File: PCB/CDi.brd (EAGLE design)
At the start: 58.5 x 61 mm, 9 parts, among them U1 SN74AHCT125N, U2 SN74AHCT125N

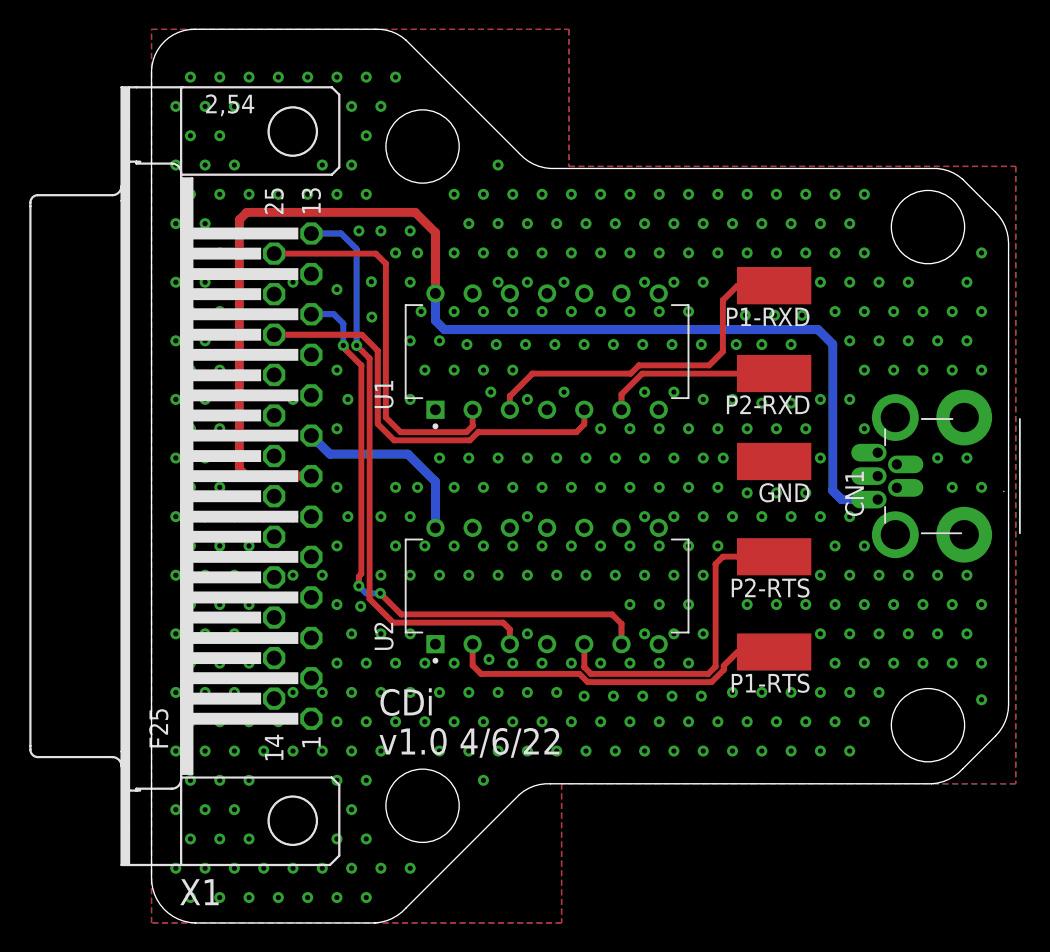
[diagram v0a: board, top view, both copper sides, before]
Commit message: CD-i PCB/BOM Update
Identified USB Mini from Digikey and add it to the BOM.

Updated the PCB to match the layout for the USB Mini Connector and added a callout on the PCB that the connector is required for 5V Power.

Updated project status to include the complete PC-FX Status.
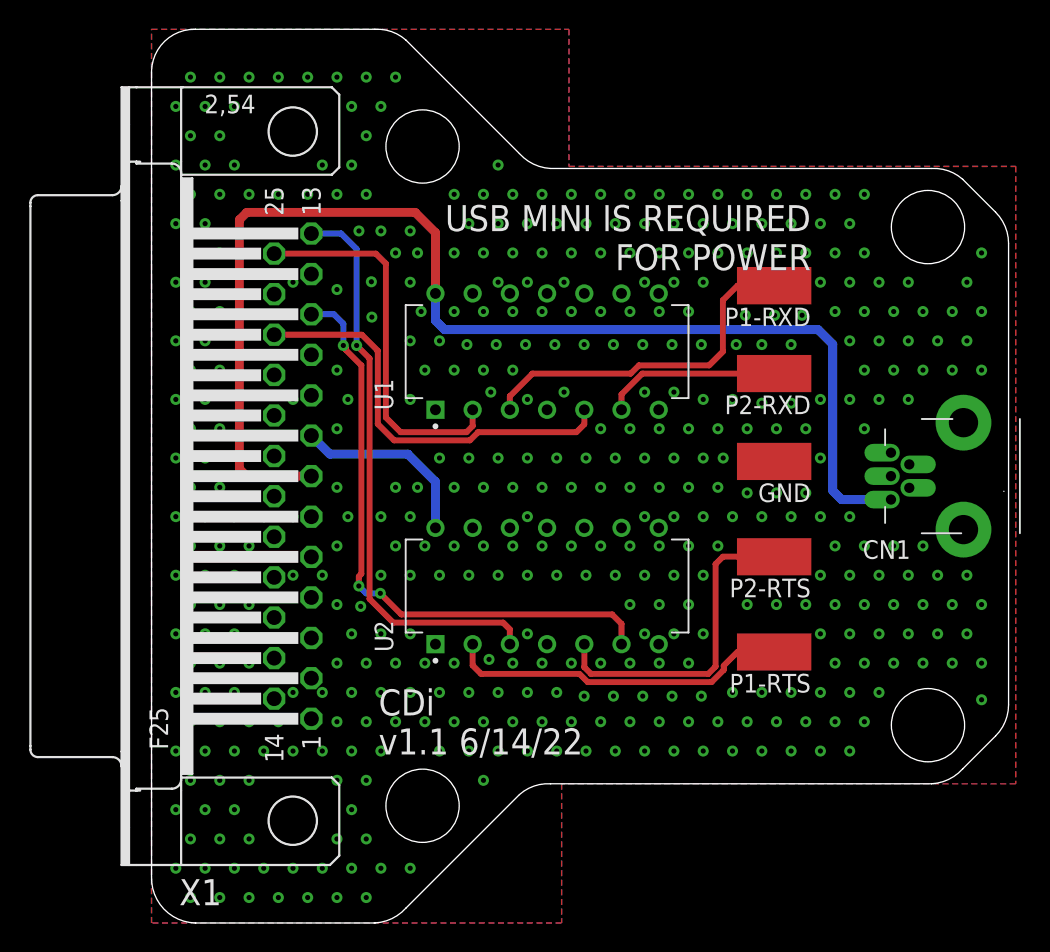
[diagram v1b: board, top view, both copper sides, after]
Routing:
- net 5VIN: track 83.4 -> 84.3 mm
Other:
- board text added: "CDi v1.1 6/14/22"
- board text added: "USB MINI IS REQUIRED FOR POWER"
- board text removed: "CDi v1.0 4/6/22"
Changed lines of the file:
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@@
 <drawing>
 <settings>
-<setting alwaysvectorfont="no"/>
+<setting alwaysvectorfont="yes"/>
 <setting verticaltext="up"/>
 </settings>
@@
 <hole x="18.5" y="8" drill="5"/>
 <text x="15.5" y="11.5" size="1.778" layer="21">CDi
-v1.0 4/6/22</text>
+v1.1 6/14/22</text>
+<text x="45" y="49" size="1.778" layer="21" rot="R180">USB MINI IS REQUIRED
+FOR POWER</text>
 </plain>
 <attributes>
@@
 </element>
 <element name="CN1" library="adafruit" package="USB-MINIB-THM" value="" x="59.373" y="30.5" smashed="yes" rot="R90">
-<attribute name="NAME" x="48.623" y="27.69" size="1.27" layer="25" font="vector" rot="R90"/>
+<attribute name="NAME" x="51.81" y="26.123" size="1.27" layer="25" font="vector" rot="R180"/>
 <attribute name="VALUE" x="61.023" y="27.19" size="1.27" layer="27" font="vector" rot="R90"/>
 </element>
@@
 <via x="54.6568" y="21.735840625" extent="1-16" drill="0.35"/>
 <via x="53.6568" y="23.735840625" extent="1-16" drill="0.35"/>
-<via x="54.6568" y="29.735840625" extent="1-16" drill="0.35"/>
-<via x="53.6568" y="31.735840625" extent="1-16" drill="0.35"/>
+<via x="50.6568" y="25.735840625" extent="1-16" drill="0.35"/>
+<via x="49.6568" y="35.735840625" extent="1-16" drill="0.35"/>
 <via x="54.6568" y="37.735840625" extent="1-16" drill="0.35"/>
 <via x="53.6568" y="39.735840625" extent="1-16" drill="0.35"/>
@@
 <via x="56.6568" y="21.735840625" extent="1-16" drill="0.35"/>
 <via x="55.6568" y="23.735840625" extent="1-16" drill="0.35"/>
-<via x="56.6568" y="29.735840625" extent="1-16" drill="0.35"/>
-<via x="55.6568" y="31.735840625" extent="1-16" drill="0.35"/>
+<via x="52.6568" y="25.735840625" extent="1-16" drill="0.35"/>
+<via x="51.6568" y="35.735840625" extent="1-16" drill="0.35"/>
 <via x="56.6568" y="37.735840625" extent="1-16" drill="0.35"/>
 <via x="55.6568" y="39.735840625" extent="1-16" drill="0.35"/>
@@
 <wire x1="19.38" y1="41.12" x2="20" y2="40.5" width="0.6096" layer="16"/>
 <wire x1="45.5" y1="40.5" x2="46.5" y2="39.5" width="0.6096" layer="16"/>
-<wire x1="47.1" y1="28.9" x2="49.573" y2="28.9" width="0.6096" layer="16"/>
+<wire x1="47.1" y1="28.9" x2="50.473" y2="28.9" width="0.6096" layer="16"/>
 <wire x1="20" y1="40.5" x2="45.5" y2="40.5" width="0.6096" layer="16"/>
 <wire x1="46.5" y1="39.5" x2="46.5" y2="29.5" width="0.6096" layer="16"/>

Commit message: Added exposed GND plane at DB25 anchors
All PCBs have been update to have exposed GND plane pads for the DB25 anchor points.

This resolves Issue 54
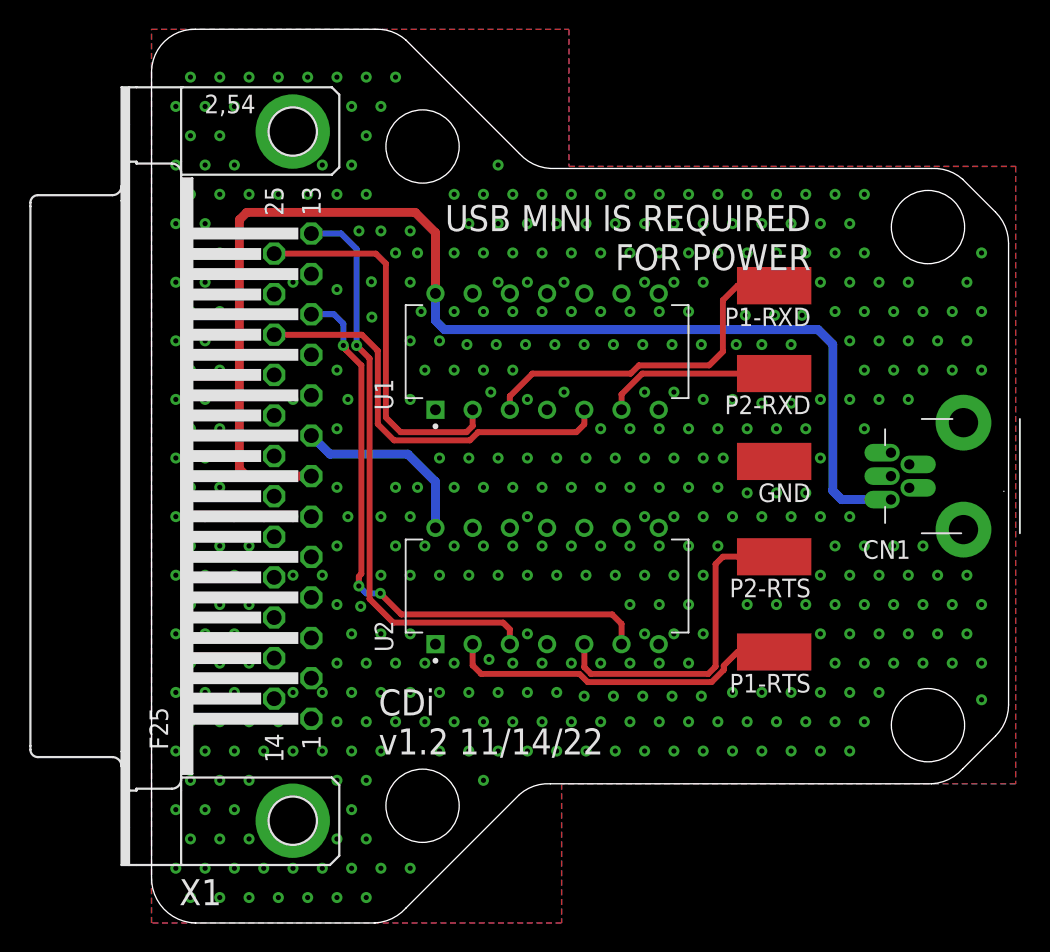
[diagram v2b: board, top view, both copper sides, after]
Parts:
- X1: device SparkFun-Retired:F25H -> SparkFun-Retired:F25HP
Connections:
- net GND: now also X1.GND1, X1.GND2
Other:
- board text added: "CDi v1.2 11/14/22"
- board text removed: "CDi v1.1 6/14/22"
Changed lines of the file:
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@@
 <drawing>
 <settings>
-<setting alwaysvectorfont="yes"/>
+<setting alwaysvectorfont="no"/>
 <setting verticaltext="up"/>
 </settings>
@@
 <hole x="18.5" y="8" drill="5"/>
 <text x="15.5" y="11.5" size="1.778" layer="21">CDi
-v1.1 6/14/22</text>
+v1.2 11/14/22</text>
 <text x="45" y="49" size="1.778" layer="21" rot="R180">USB MINI IS REQUIRED
 FOR POWER</text>
@@
 <attribute name="PURCHASE-URL" value="https://pricing.snapeda.com/search/part/SN74AHCT125N/?ref=eda" x="65.1" y="47.13" size="1.778" layer="27" rot="R90" display="off"/>
 </element>
-<element name="X1" library="SparkFun-Retired" package="F25H" value="" x="9.64" y="30.5" smashed="yes" rot="R90">
+<element name="X1" library="SparkFun-Retired" package="F25HP" value="" x="9.64" y="30.5" smashed="yes" rot="R90">
 <attribute name="NAME" x="4.789" y="2.99" size="1.778" layer="25" ratio="10" rot="R180"/>
 <attribute name="VALUE" x="-4.33" y="22.118" size="1.778" layer="27" ratio="10" rot="R90"/>
@@
 <vertex x="27.99" y="0"/>
 </polygon>
-<contactref element="X1" pad="4"/>
-<contactref element="X1" pad="5"/>
-<contactref element="X1" pad="6"/>
-<contactref element="X1" pad="9"/>
-<contactref element="X1" pad="15"/>
-<contactref element="X1" pad="16"/>
 <contactref element="U1" pad="9"/>
 <contactref element="U1" pad="12"/>
 <contactref element="U2" pad="9"/>
-<contactref element="X1" pad="2"/>
-<contactref element="X1" pad="3"/>
-<contactref element="X1" pad="17"/>
 <contactref element="CN1" pad="GND"/>
 <via x="2.6568" y="1.735840625" extent="1-16" drill="0.35"/>
@@
 <via x="55.6568" y="43.735840625" extent="1-16" drill="0.35"/>
 <via x="56.6568" y="45.735840625" extent="1-16" drill="0.35"/>
+<contactref element="X1" pad="GND2"/>
+<contactref element="X1" pad="GND1"/>
+<contactref element="X1" pad="4"/>
+<contactref element="X1" pad="5"/>
+<contactref element="X1" pad="6"/>
+<contactref element="X1" pad="9"/>
+<contactref element="X1" pad="15"/>
+<contactref element="X1" pad="16"/>
+<contactref element="X1" pad="2"/>
+<contactref element="X1" pad="3"/>
+<contactref element="X1" pad="17"/>
 </signal>
 <signal name="5VIN">

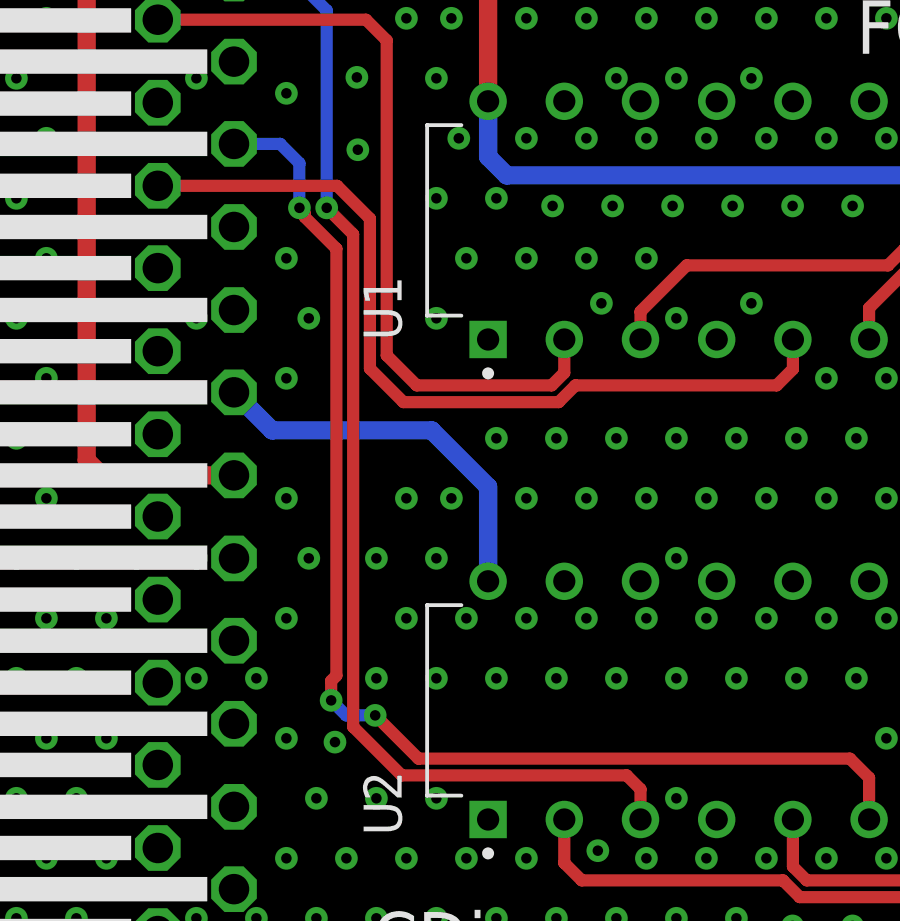
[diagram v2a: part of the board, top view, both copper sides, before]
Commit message: Silkscreen Update, Library Add, Datasheet Add
Updated the silkscreen on all PCBs that used the SN74 components as there was not orientation marker on the silkscreen.

Added Modified SN74 libraries and VB Cable Pinout image
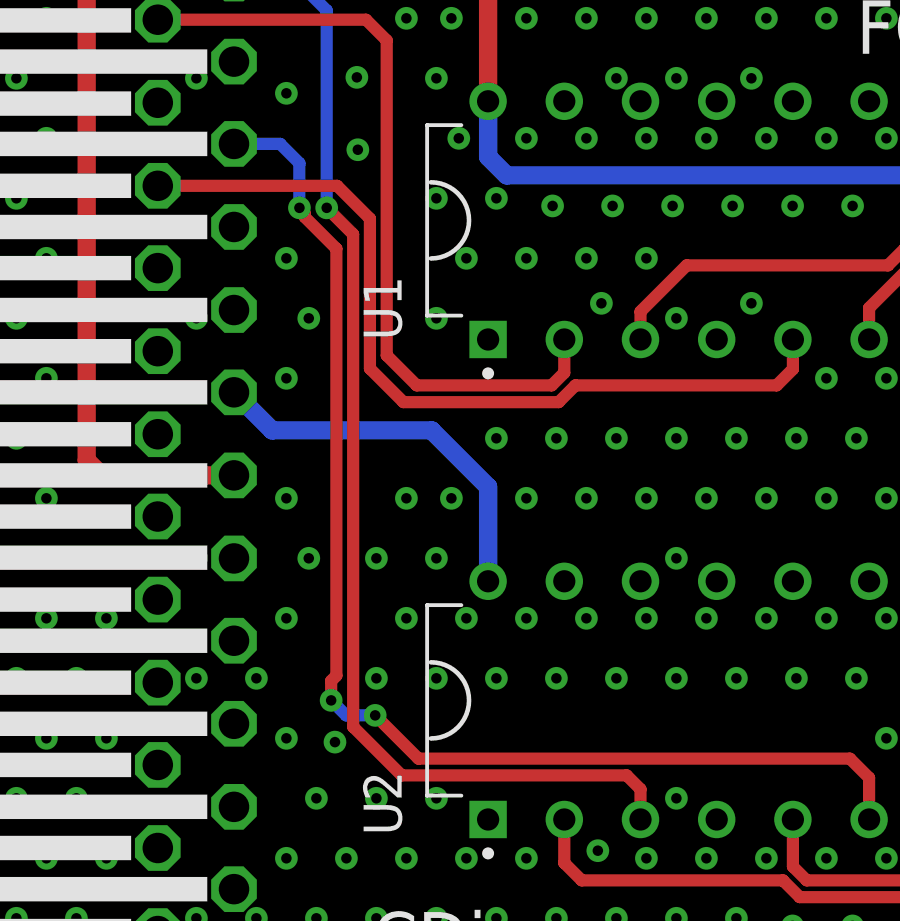
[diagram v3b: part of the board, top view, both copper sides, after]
